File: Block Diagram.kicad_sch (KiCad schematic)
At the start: 0 parts

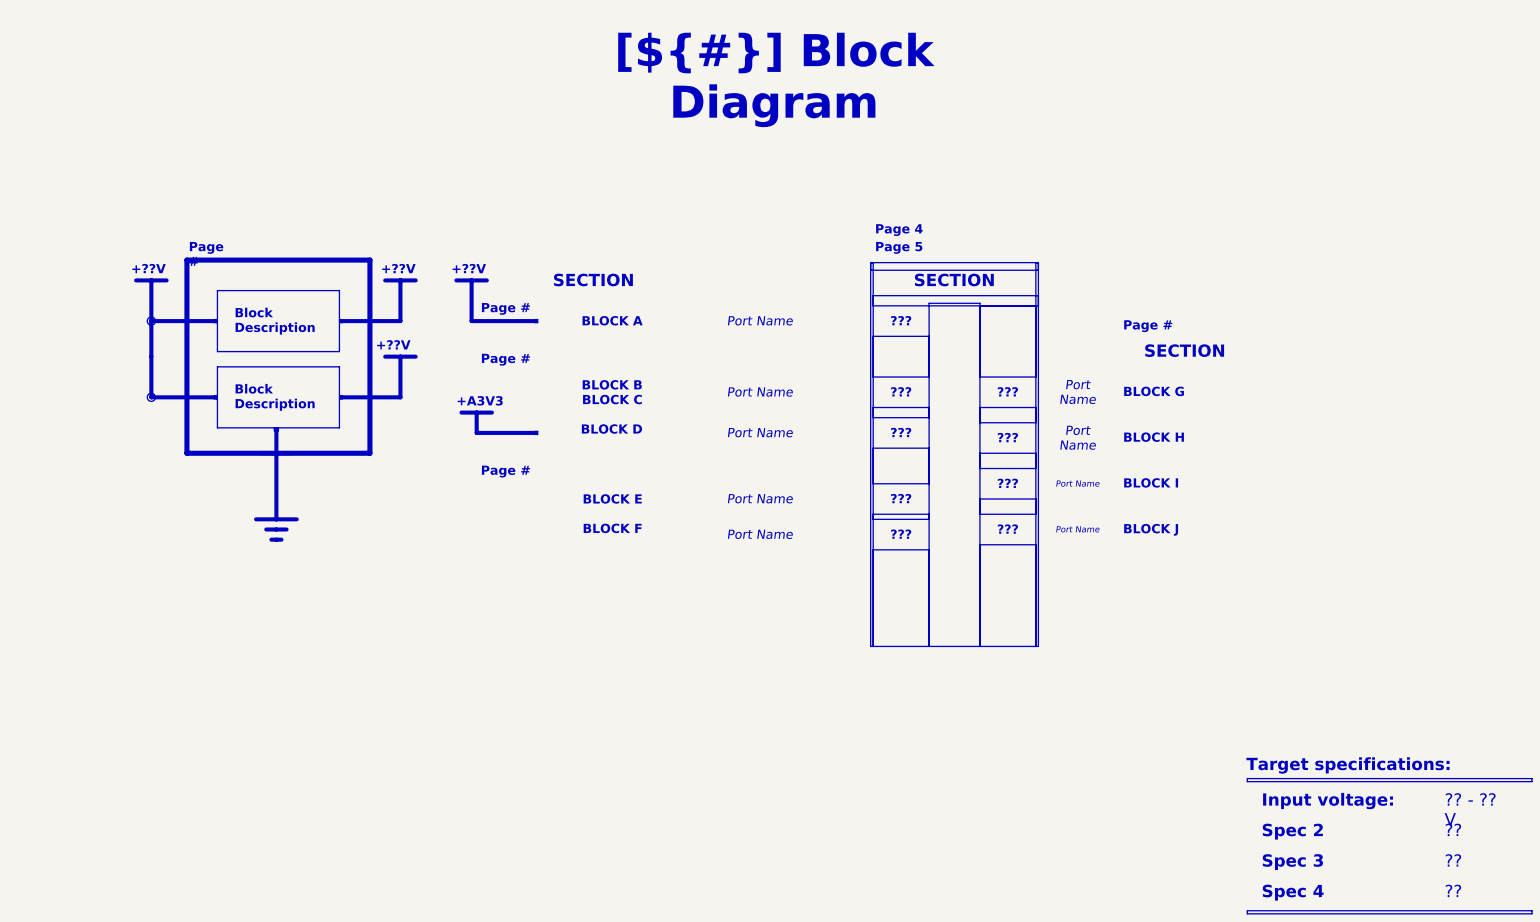
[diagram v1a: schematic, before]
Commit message: PCB[Routing, Mechanical, Silk]: Inital routing, Finalized mounting points and board to board connector reltive posision, and inital silkscreen. SCH[Labels]: Updated labels to match BMS_Slave board.
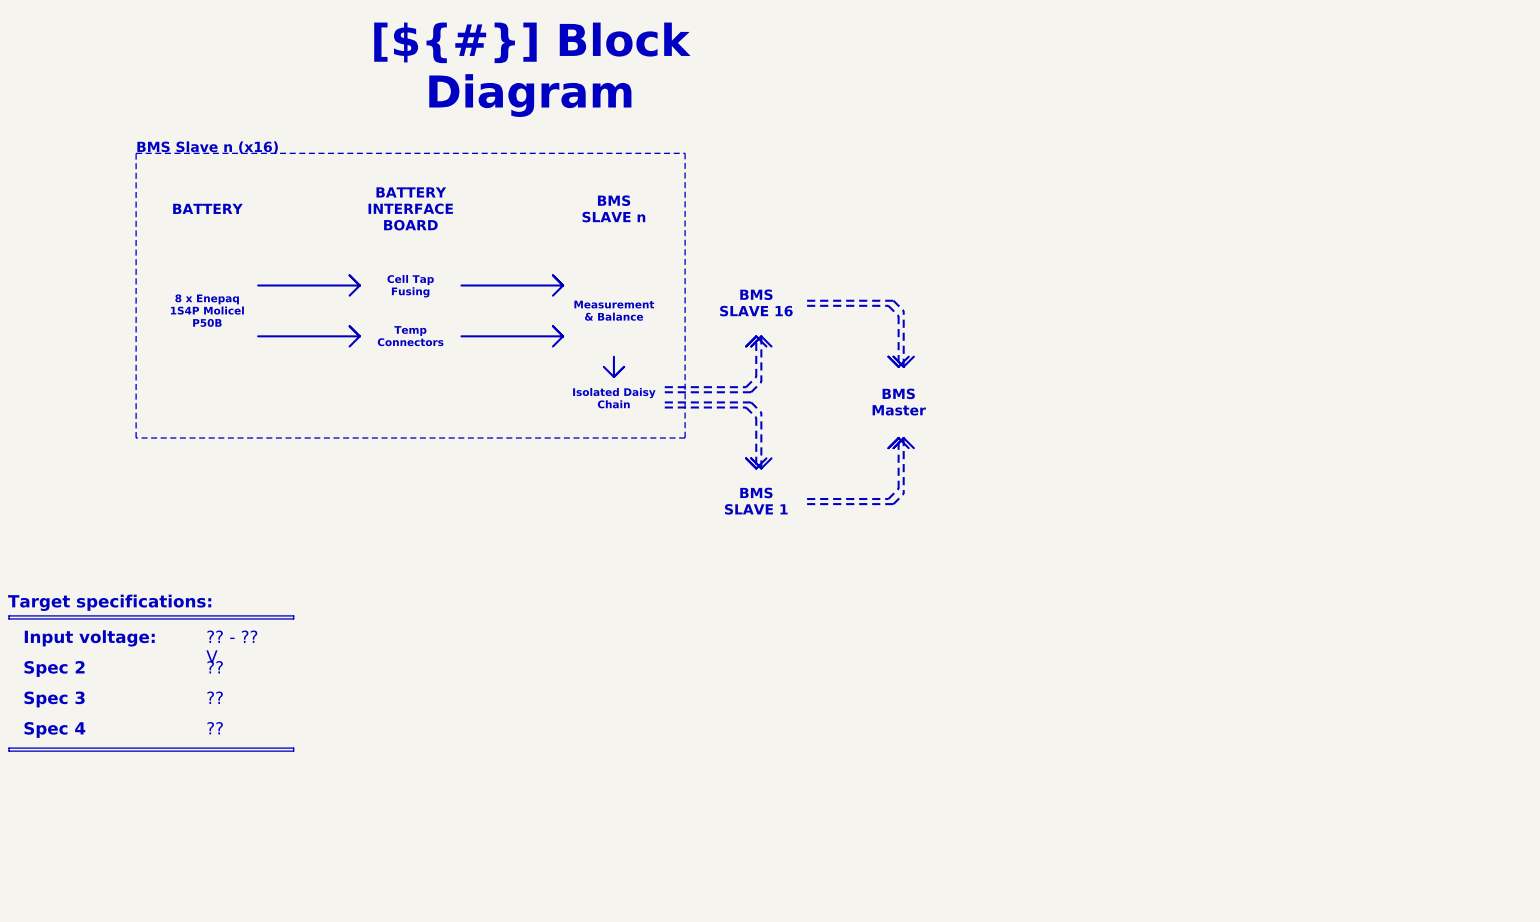
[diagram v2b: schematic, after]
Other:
- note added: "BMS Slave n (x16)"
- note removed: "+??V"
- note removed: "+A3V3"
